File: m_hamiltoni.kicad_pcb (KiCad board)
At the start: 2 copper layers, 39 parts, among them J1 MJ-4PP-9, J3 OLED, U1 ProMicro_r

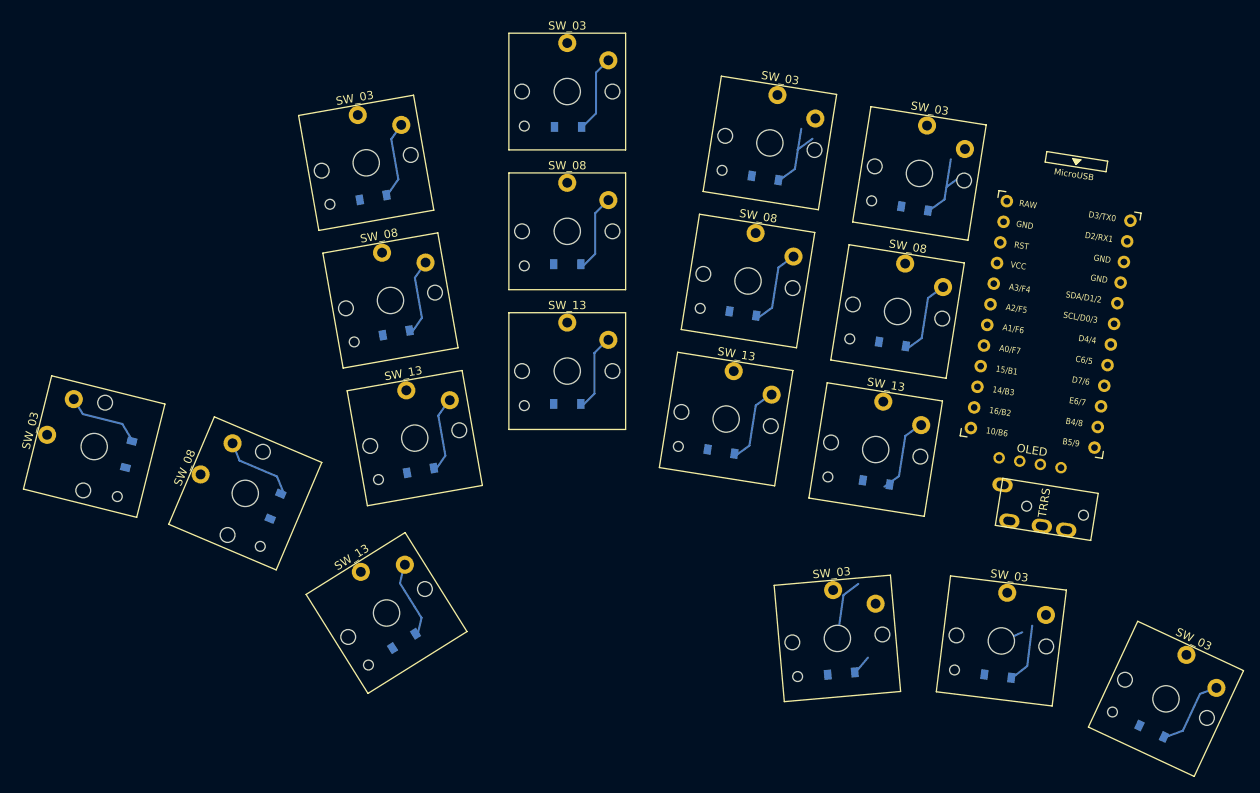
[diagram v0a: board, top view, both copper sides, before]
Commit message: Draft a more compact layout
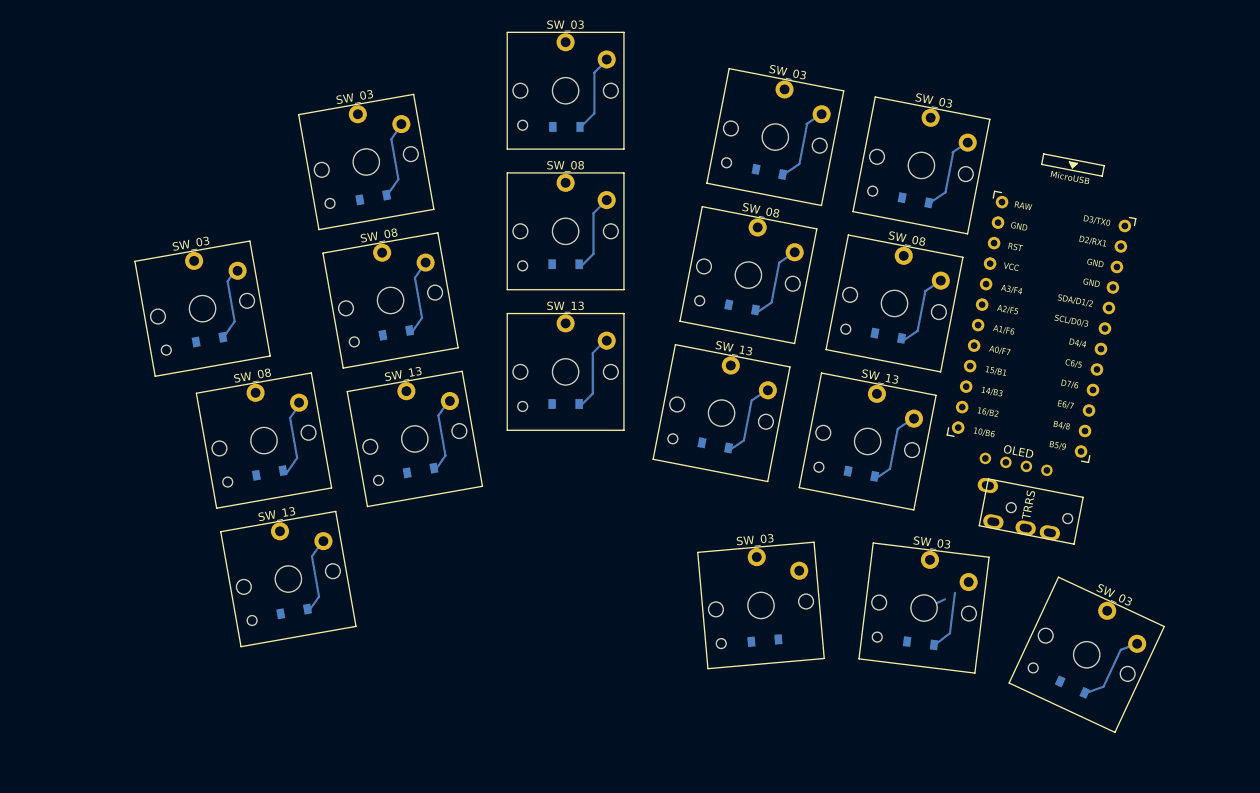
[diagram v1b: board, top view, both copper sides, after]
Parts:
- removed the D_13 at (-49.2, 30.5)
- removed the D_13 at (-68.1, 26.8)
- removed the SW_03 at (-34.0, 49.8)
- removed the SW_03 at (-14.0, 56.9)
- removed the SW_03 at (-44.0, -7.04)
- removed the SW_08 at (-46.6, 9.75)
- removed the SW_08 at (-64.8, 6.04)
- removed the SW_13 at (-105.4, 25.2)
- removed the SW_13 at (-49.3, 26.5)
- removed the SW_13 at (-67.5, 22.8)
- added D_13: 1N4148, Diode_SMD:D_SOD-123, B.Cu at (-51.0, 29.5)
- added D_13: 1N4148, Diode_SMD:D_SOD-123, B.Cu at (-68.8, 26.0)
- added SW_03: CHOC_V1, Switch_Keyboard_Kailh:SW_Kailh_Choc_V1_1.00u, F.Cu at (-43.7, -8.01)
- added SW_03: CHOC_V1, Switch_Keyboard_Kailh:SW_Kailh_Choc_V1_1.00u, F.Cu at (-43.4, 45.8)
- added SW_03: CHOC_V1, Switch_Keyboard_Kailh:SW_Kailh_Choc_V1_1.00u, F.Cu at (-23.6, 51.5)
- added SW_08: CHOC_V1, Switch_Keyboard_Kailh:SW_Kailh_Choc_V1_1.00u, F.Cu at (-47.0, 8.77)
- added SW_08: CHOC_V1, Switch_Keyboard_Kailh:SW_Kailh_Choc_V1_1.00u, F.Cu at (-64.8, 5.32)
- added SW_13: CHOC_V1, Switch_Keyboard_Kailh:SW_Kailh_Choc_V1_1.00u, F.Cu at (-50.3, 25.6)
- added SW_13: CHOC_V1, Switch_Keyboard_Kailh:SW_Kailh_Choc_V1_1.00u, F.Cu at (-105.4, 25.3)
- added SW_13: CHOC_V1, Switch_Keyboard_Kailh:SW_Kailh_Choc_V1_1.00u, F.Cu at (-68.0, 22.1)
- moved SW_03 21.3 mm to (-131.2, 9.41), turned to 10 degrees
- moved D_03 17.1 mm to (-130.3, 13.2), turned to 10 degrees
- moved D_13 13.8 mm to (-120.0, 46.2), turned to 10 degrees
- moved SW_13 12.6 mm to (-120.7, 42.3), turned to 10 degrees
- moved D_03 11.0 mm to (-25.4, 55.4)
- moved D_03 10.2 mm to (-43.8, 50.1)
- moved D_03 10.1 mm to (-62.8, 49.8)
- moved SW_03 10.1 mm to (-63.3, 45.5)
- moved SW_08 6.81 mm to (-123.7, 25.5), turned to 10 degrees
- moved D_08 4.11 mm to (-123.0, 29.4), turned to 10 degrees
- moved J1 1.99 mm to (-24.5, 35.2), turned to 259 degrees
- moved J3 1.71 mm to (-32.2, 28.3), turned to 349 degrees
- moved U1 1.16 mm to (-29.2, 12.1), turned to 349 degrees
- moved D_08 1.12 mm to (-47.8, 12.7), turned to 349 degrees
- moved D_03 1.00 mm to (-44.5, -3.77), turned to 349 degrees
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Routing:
- net (no net): track 171.2 -> 161.7 mm

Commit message: Draft an outline for the PCB
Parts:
- moved U1 1.87 mm to (-28.9, 10.3)
- moved J1 0.52 mm to (-24.6, 35.7)
- moved J3 0.10 mm to (-32.3, 28.4)
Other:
- board outline added: 129.1 x 88.3 mm
